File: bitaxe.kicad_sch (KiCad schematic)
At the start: 92 parts, among them IC1 BM1387, IC2 BM1387, IC3 MIC5317, IC4 MIC5317, J2 Conn_01x02, J3 Conn_01x05, J4 Conn_01x02, J5 Conn_01x03, Y1 25MHz

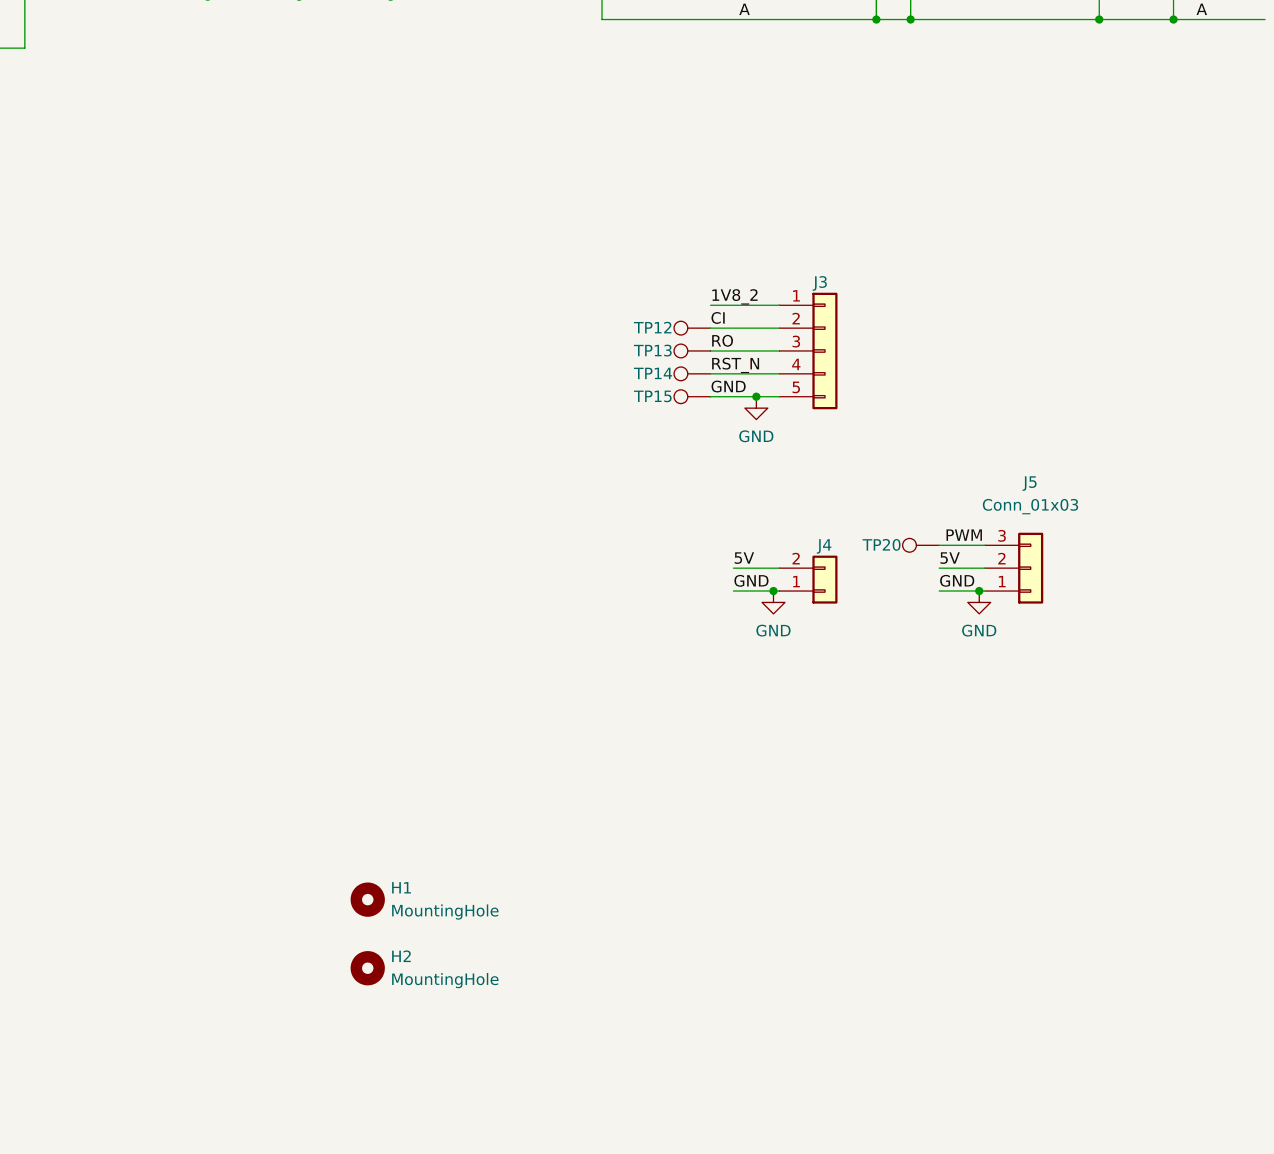
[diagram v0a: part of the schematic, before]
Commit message: change both vreg voltage divider to 100 ohm parts (and updated BOM)
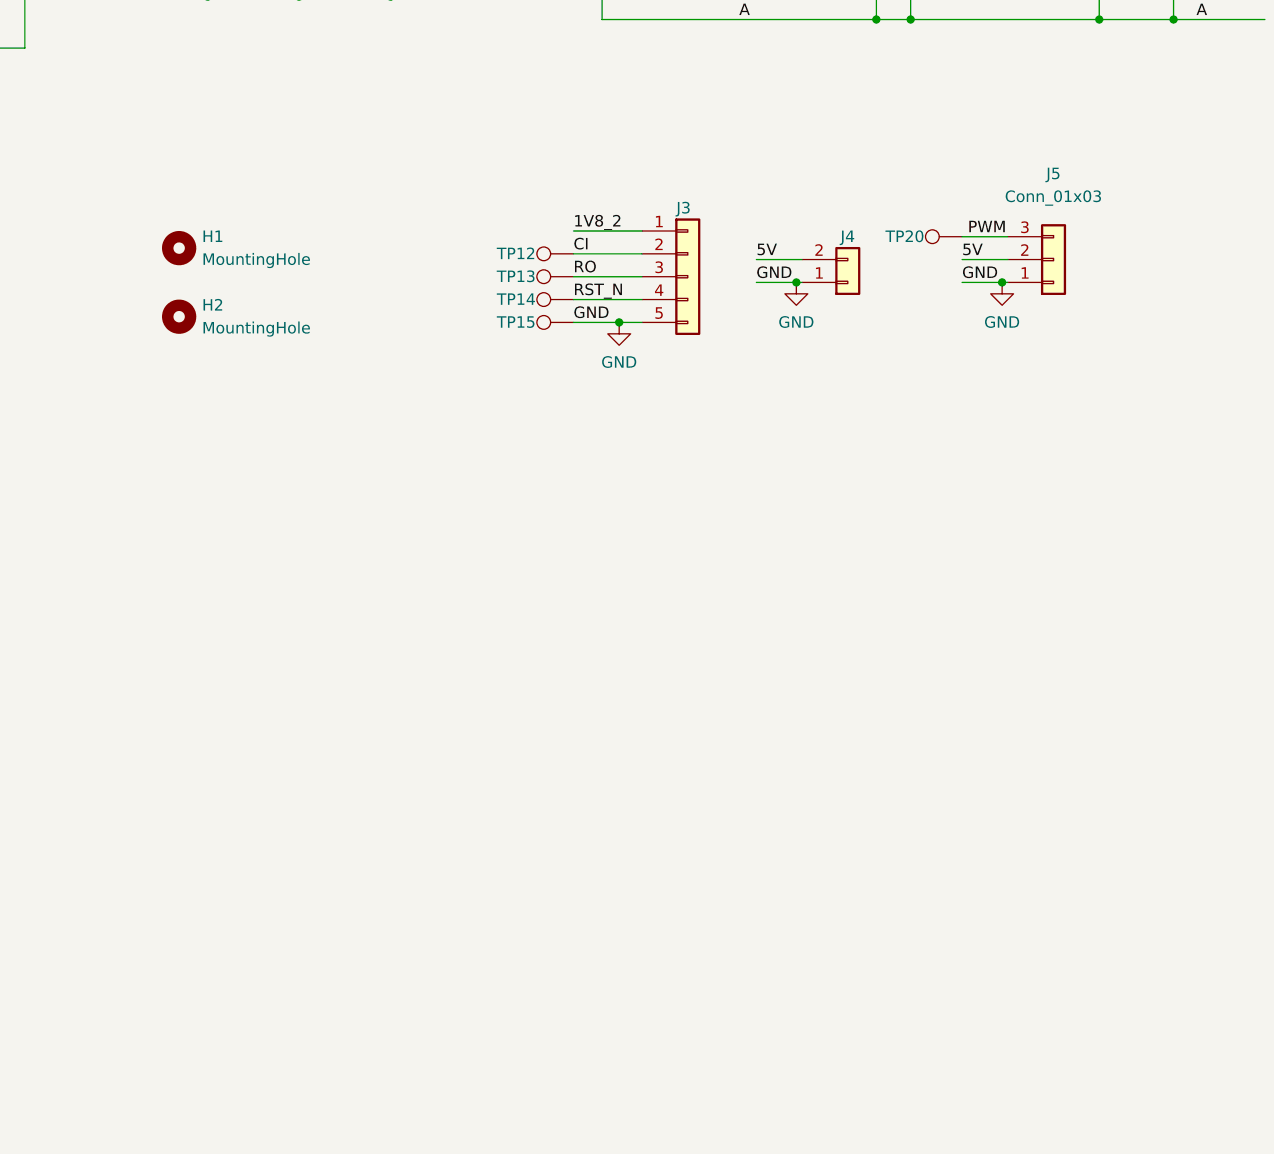
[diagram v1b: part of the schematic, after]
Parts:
- C3: DK (none) -> 1292-1639-1-ND
- JP1, JP2, JP3, JP4, JP5, JP6, JP7, JP8: DNP (none) -> T
- R19, R21: DK RMCF0402FT12K4CT-ND -> RMCF0402FT100RCT-ND
- R20: footprint DayMiner:C0402 -> DayMiner:R0402; DK RMCF0402FT10K0CT-ND -> RMCF0402FT100RCT-ND
- R22: DK RMCF0402FT10K0CT-ND -> RMCF0402FT100RCT-ND
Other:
- moved on the sheet: H1, H2, J3, J4, J5, TP12, TP13, TP14, TP15, TP20

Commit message: schematic cleanup
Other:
- moved on the sheet: C1, C10, C11, C12, C14, C15, C16, C17, C18, C19, C2, C20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

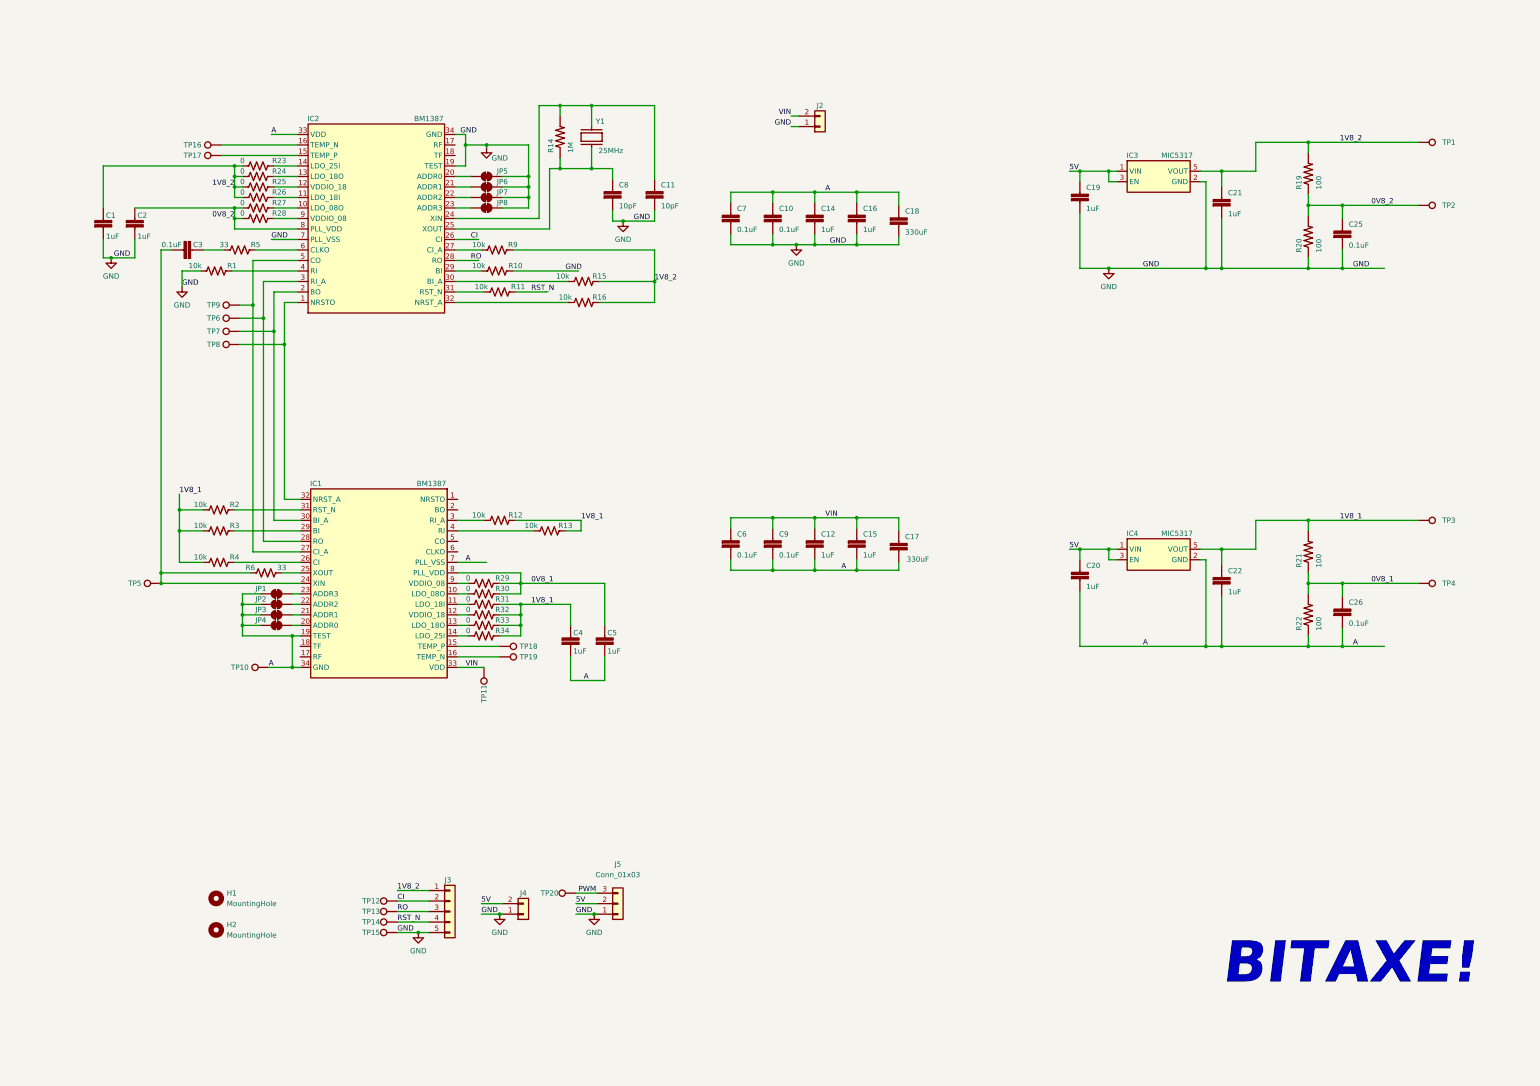
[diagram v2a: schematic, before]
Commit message: updated silkscreen for #1. Added some 1.5mm alignment pin holes in the stencil and PCB
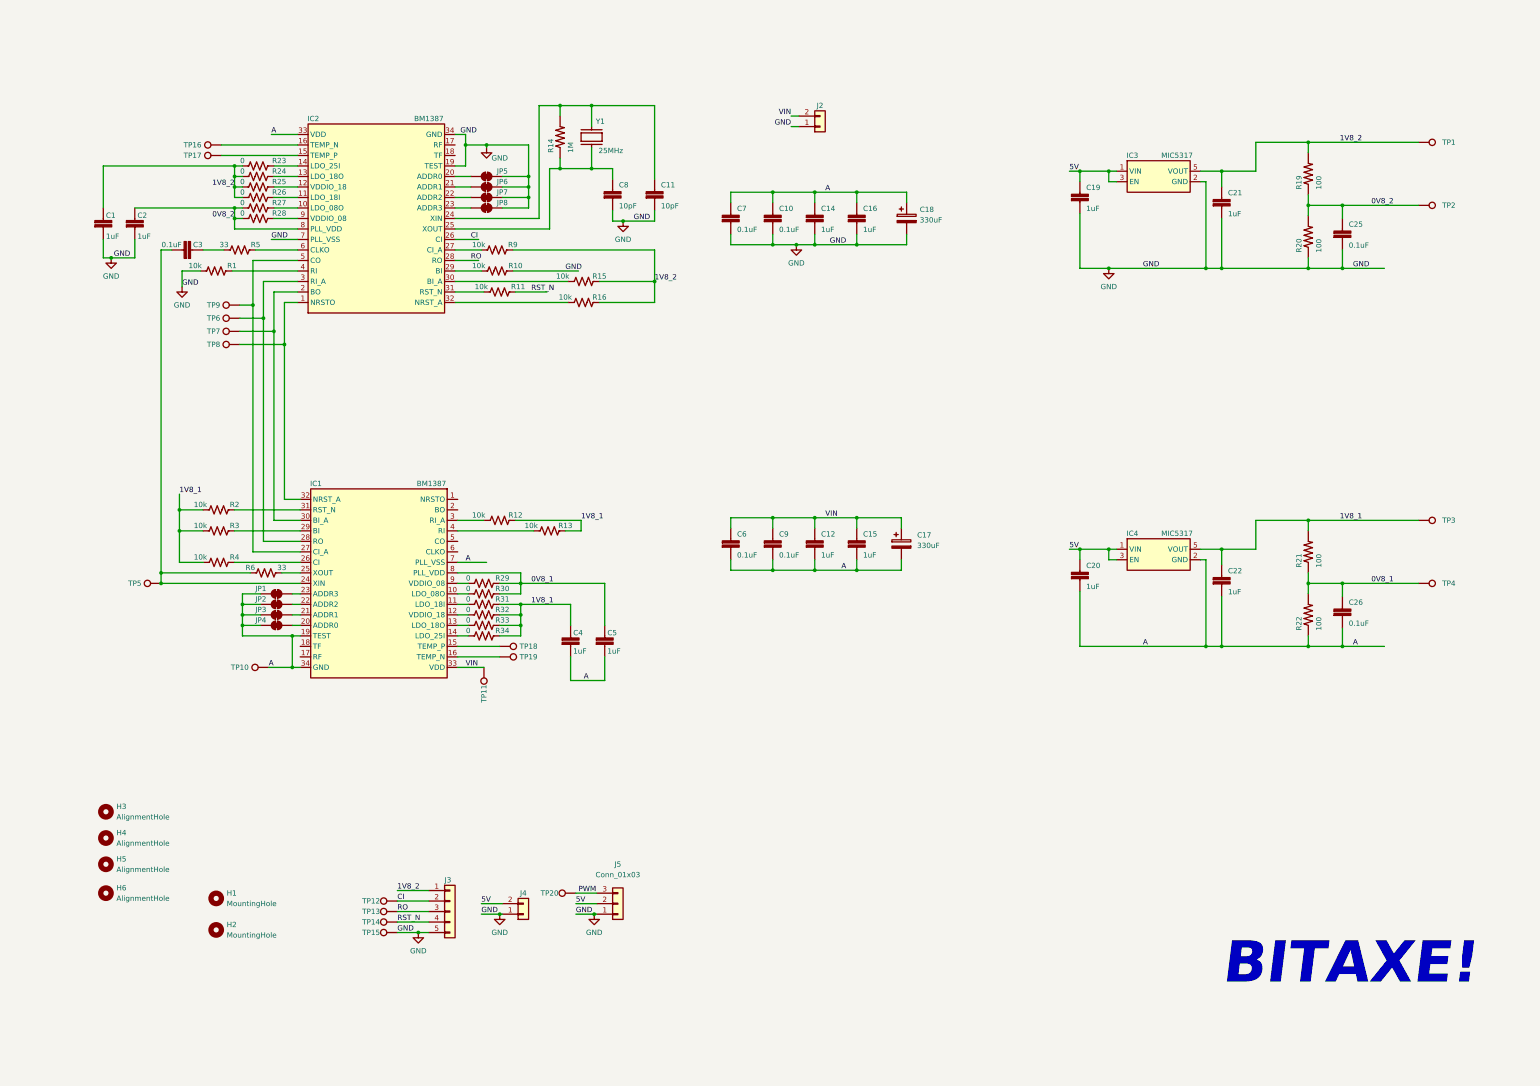
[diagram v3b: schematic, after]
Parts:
- removed C17, C18: 330uF, Capacitor_Tantalum_SMD:CP_EIA-7343-31_Kemet-D_Pad2.25x2.55mm_HandSolder, symbol DayMiner-eagle-import:CAP0402
- added C17, C18: 330uF, Capacitor_Tantalum_SMD:CP_EIA-7343-31_Kemet-D_Pad2.25x2.55mm_HandSolder_flip, symbol Device:C_Polarized
- added H3, H4, H5, H6: AlignmentHole, DayMiner:alignment_pin_1.5mm, symbol Mechanical:MountingHole
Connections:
- net A: now also C17.2, C18.1
- net GND: now also C18.2
- net VIN: now also C17.1

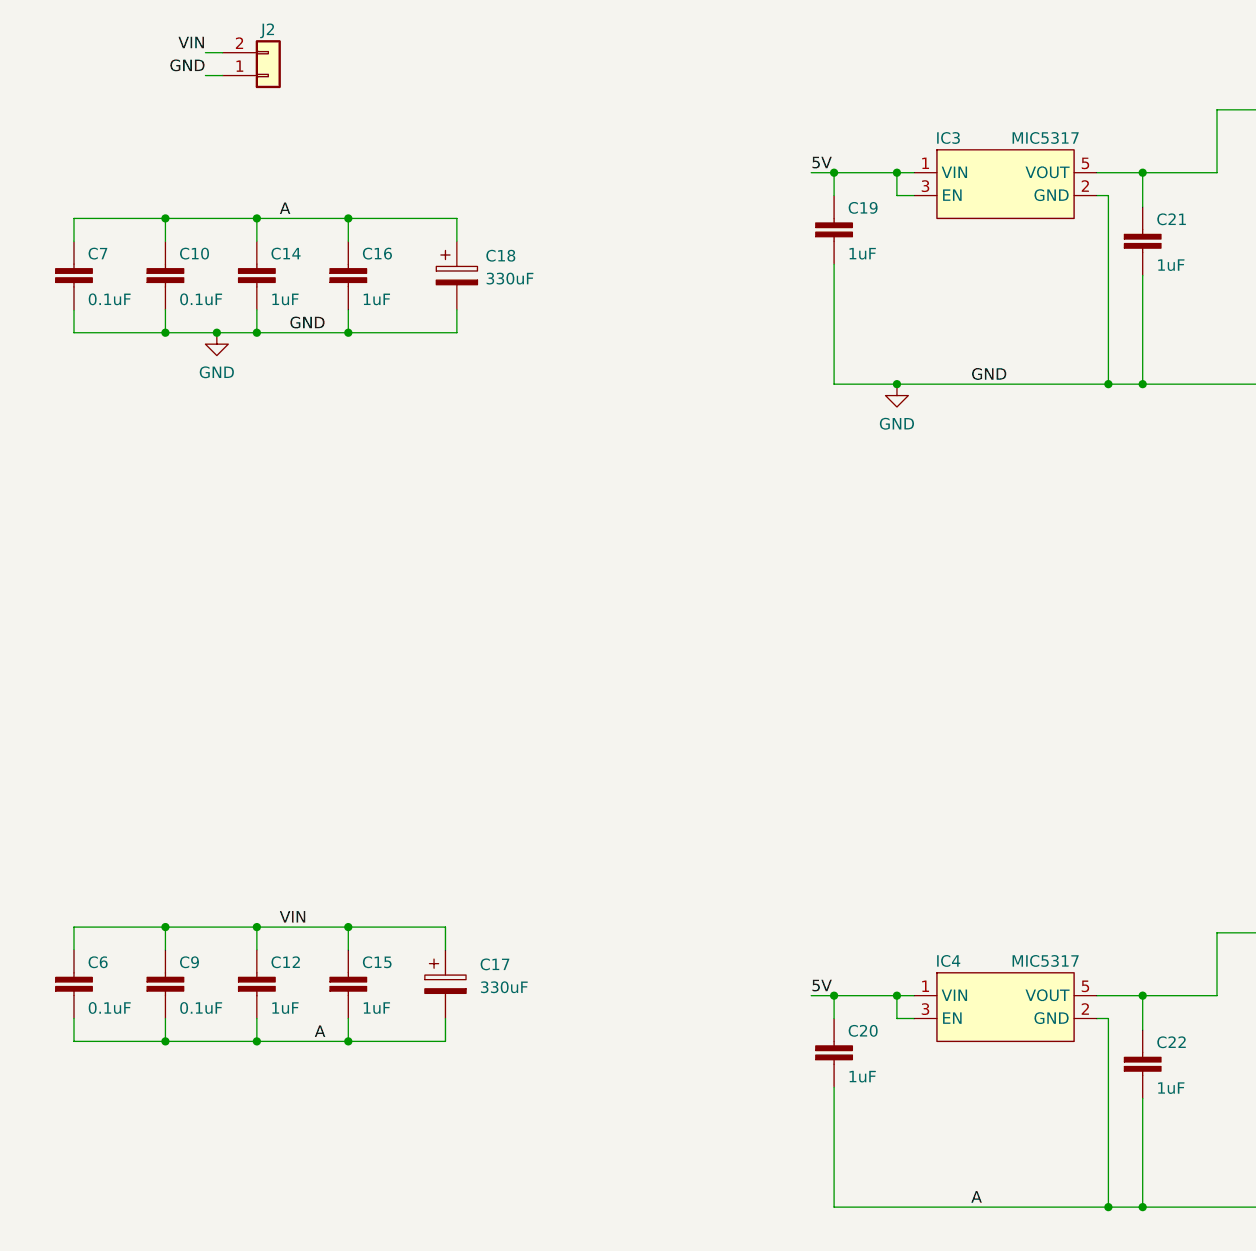
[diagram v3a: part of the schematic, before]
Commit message: added VIN spade connectors for #6. moved the 5V pinheader around the corner. fixed the part numbers on R19-R22. Switched to in-stock LDOs for IC4 and IC5
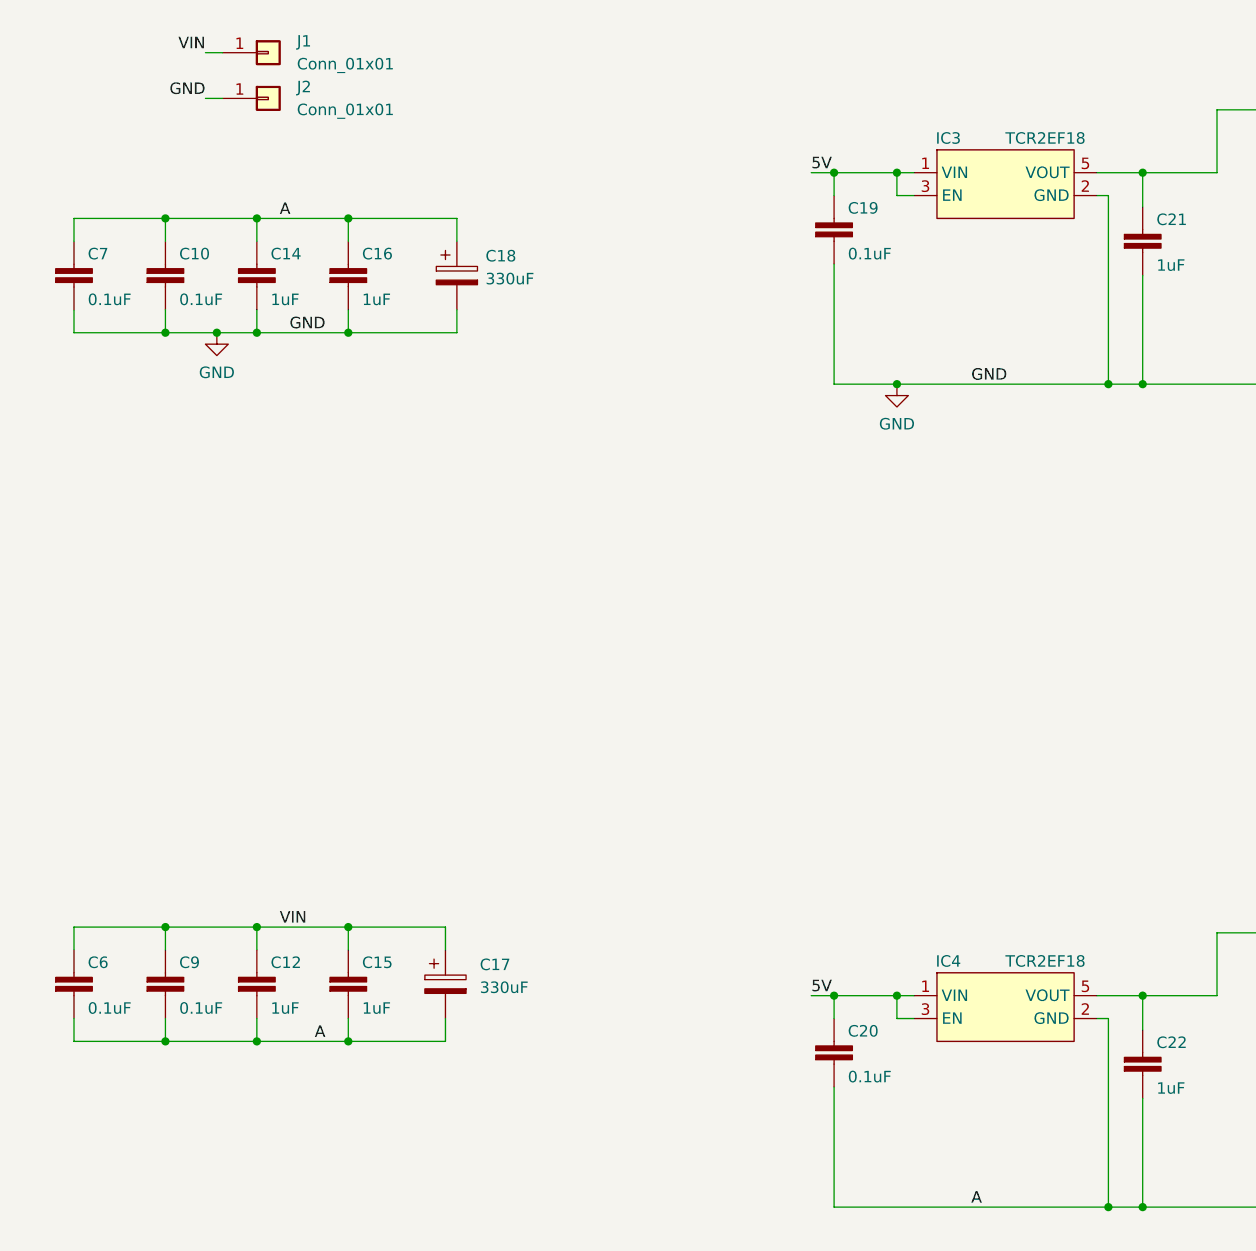
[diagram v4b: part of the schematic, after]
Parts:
- removed J2: Conn_01x02, Connector_PinHeader_2.54mm:PinHeader_1x02_P2.54mm_Vertical, symbol Connector_Generic:Conn_01x02
- added J1, J2: Conn_01x01, DayMiner:63862-1, symbol Connector_Generic:Conn_01x01
- C19, C20: value 1uF -> 311-3342-1-ND; DK 587-5514-1-ND -> 1292-1639-1-ND
- IC3, IC4: value MIC5317 -> TCR2EF18; footprint DayMiner:SOT23-5 -> DayMiner:TCR2EF18; DK MIC5317-1.8YM5-TR-ND -> TCR2EF18LM(CTCT-ND; PARTNO MIC5317-1.8YM5-TR -> TCR2EF18,LM(CT
- R19: value RMCF0402FT12K4CT-ND -> 100; PARTNO (none) -> RMCF0402FT100R
- R20, R22: value RMCF0402FT10K0CT-ND -> 100
- R21: value RMCF0402FT12K4CT-ND -> 100
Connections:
- net GND: now also J2.1 (Pin_1)
- net VIN: now also J1.1 (Pin_1)

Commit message: added v2 BOM and gerbers
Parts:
- added TP21, TP22, TP23, TP24: TestPoint, TestPoint:TestPoint_Pad_D1.5mm, symbol Connector:TestPoint
- J5: footprint Connector_PinHeader_2.54mm:PinHeader_1x03_P2.54mm_Vertical -> Connector_Molex:Molex_KK-254_AE-6410-03A_1x03_P2.54mm_Vertical; DK (none) -> WM4201-ND; PARTNO (none) -> 0022232031
- R1, R10, R11, R12, R13, R15, R16, R2, R3, R4, R9: DK (none) -> RMCF0402FT10K0CT-ND
- R23, R24, R25, R26, R27, R28, R29, R30, R31, R32, R33, R34: DK (none) -> YAG1279CT-ND
- R5, R6: DK (none) -> 311-33.0LRCT-ND
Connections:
- net at IC1.1 (NRSTO): now also TP21.1
- net at IC1.2 (BO): now also TP22.1
- net at IC1.5 (CO): now also TP23.1
- net at IC1.6 (CLKO): now also TP24.1
